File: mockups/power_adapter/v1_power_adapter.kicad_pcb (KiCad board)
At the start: 2 copper layers, 49.5 x 24.1 mm, 20 parts, among them J1 Barrel_Jack, J2 Conn_02x07_Odd_Even, U1 L7805, U2 LT1963EQ, U3 LT1963EQ

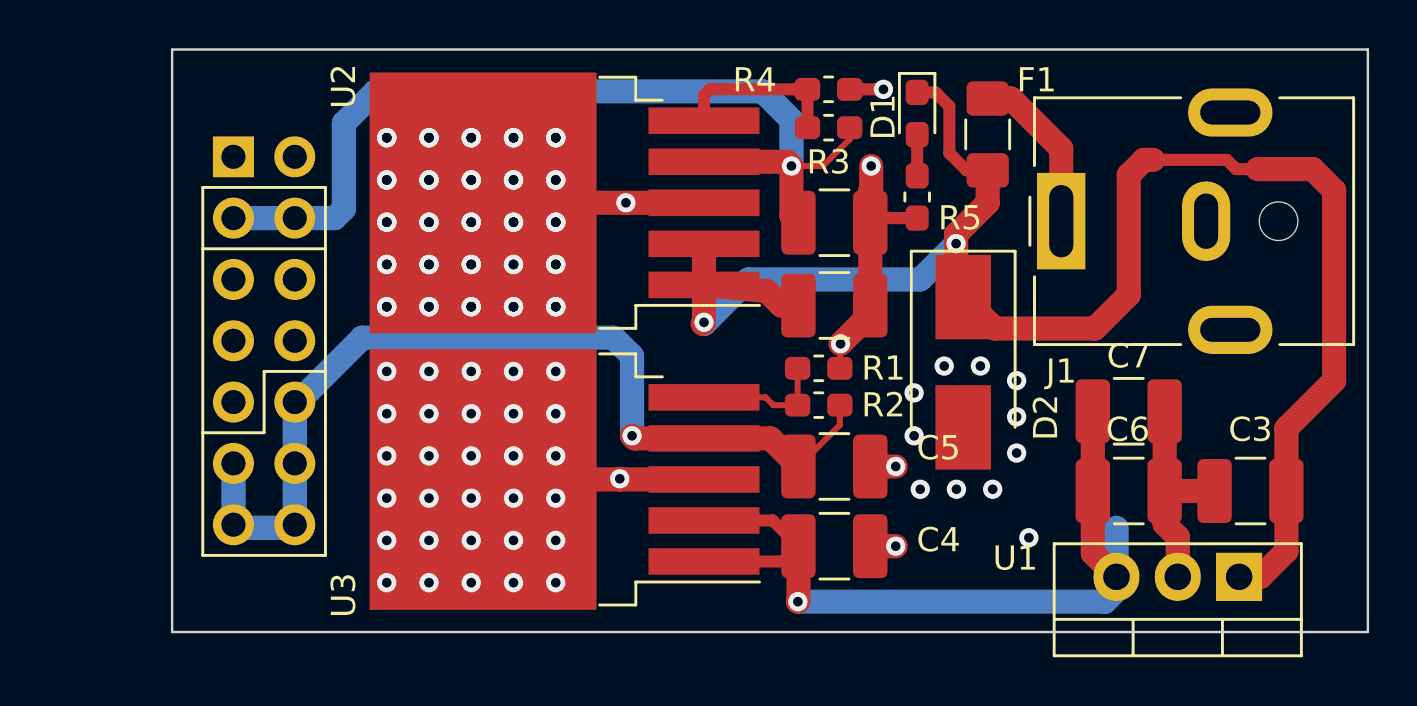
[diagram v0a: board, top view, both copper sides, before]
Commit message: Add jumpers for current measurement
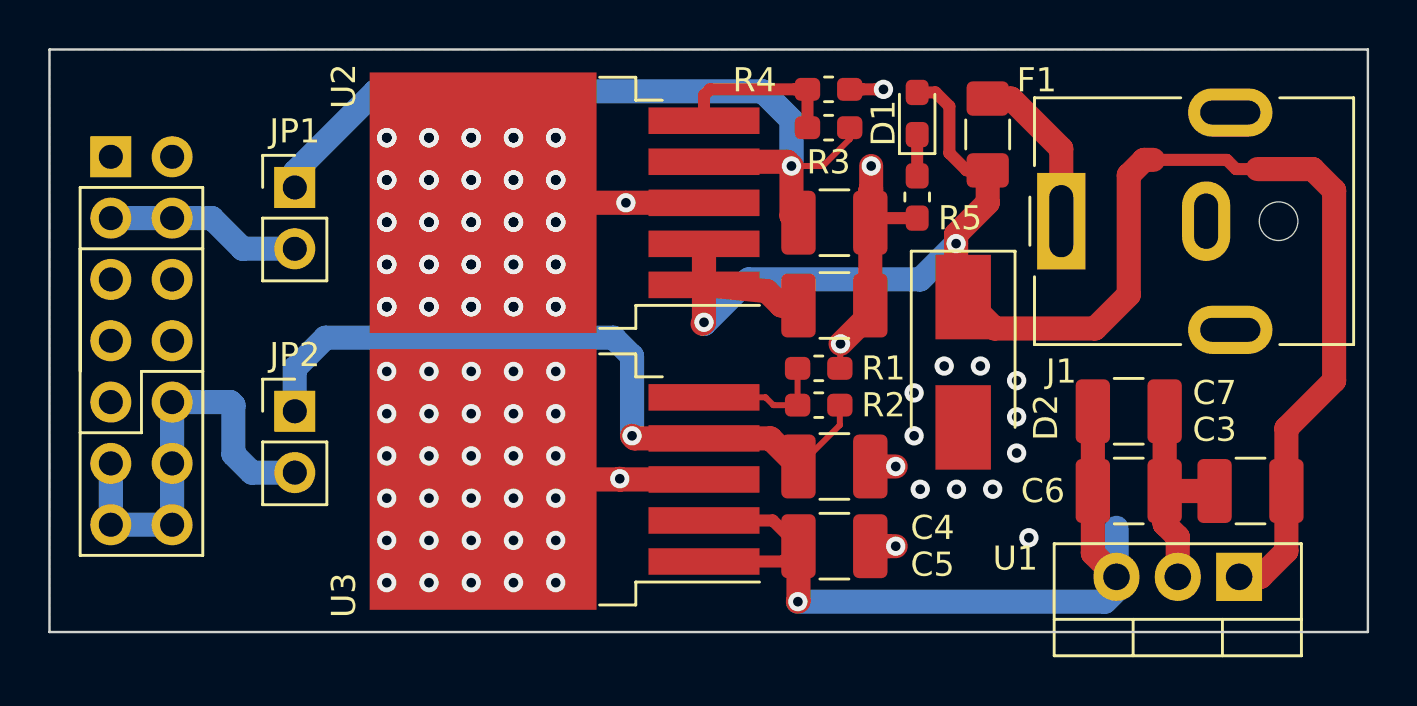
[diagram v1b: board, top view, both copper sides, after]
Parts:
- added JP1: Jumper, Connector_PinHeader_2.54mm:PinHeader_1x02_P2.54mm_Vertical, F.Cu at (129.5, 89.5)
- added JP2: Jumper, Connector_PinHeader_2.54mm:PinHeader_1x02_P2.54mm_Vertical, F.Cu at (129.5, 98.8)
- moved J2 5.08 mm to (121.9, 88.3)
- turned D1 to 90 degrees
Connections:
- C1 pad 1: /7.5V -> /7V5
- D1 pad 1: /9V_FUSED -> Net-(D1-Pad1)
- D1 pad 2: Net-(D1-Pad2) -> /9V_FUSED
- J2 pad 10: /1V2 -> /1V2_JUMP
- J2 pad 11: /1V2 -> /1V2_JUMP
- J2 pad 12: /1V2 -> /1V2_JUMP
- J2 pad 13: /1V2 -> /1V2_JUMP
- J2 pad 14: /1V2 -> /1V2_JUMP
- J2 pad 3: /7.5V -> /7V5_JUMP
- J2 pad 4: /7.5V -> /7V5_JUMP
- R3 pad 1: /7.5V -> /7V5
- R5 pad 1: Net-(D1-Pad2) -> Net-(D1-Pad1)
- U2 pad 4: /7.5V -> /7V5
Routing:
- net /7.5V: track 40.4 -> 0.00 mm, vias 1 -> 0
- net /7V5: track 0.00 -> 35.6 mm, vias 0 -> 1
- net /1V2_JUMP: track 0.00 -> 18.3 mm
- net /1V2: track 39.8 -> 30.6 mm
- net /7V5_JUMP: track 0.00 -> 8.27 mm
- net Net-(D1-Pad2): track 1.71 -> 0.00 mm
- net Net-(D1-Pad1): track 0.00 -> 1.71 mm
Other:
- board size 49.5 x 24.1 mm -> 54.6 x 24.1 mm
